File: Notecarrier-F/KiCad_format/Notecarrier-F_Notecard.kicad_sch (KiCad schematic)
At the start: 20 parts, among them J5 NanoSIM - SF72S006VBAR2500, J6 MDT420E01001, SW1 CJS-1200TA, SW2 PTS810SJK250SMTRLFS

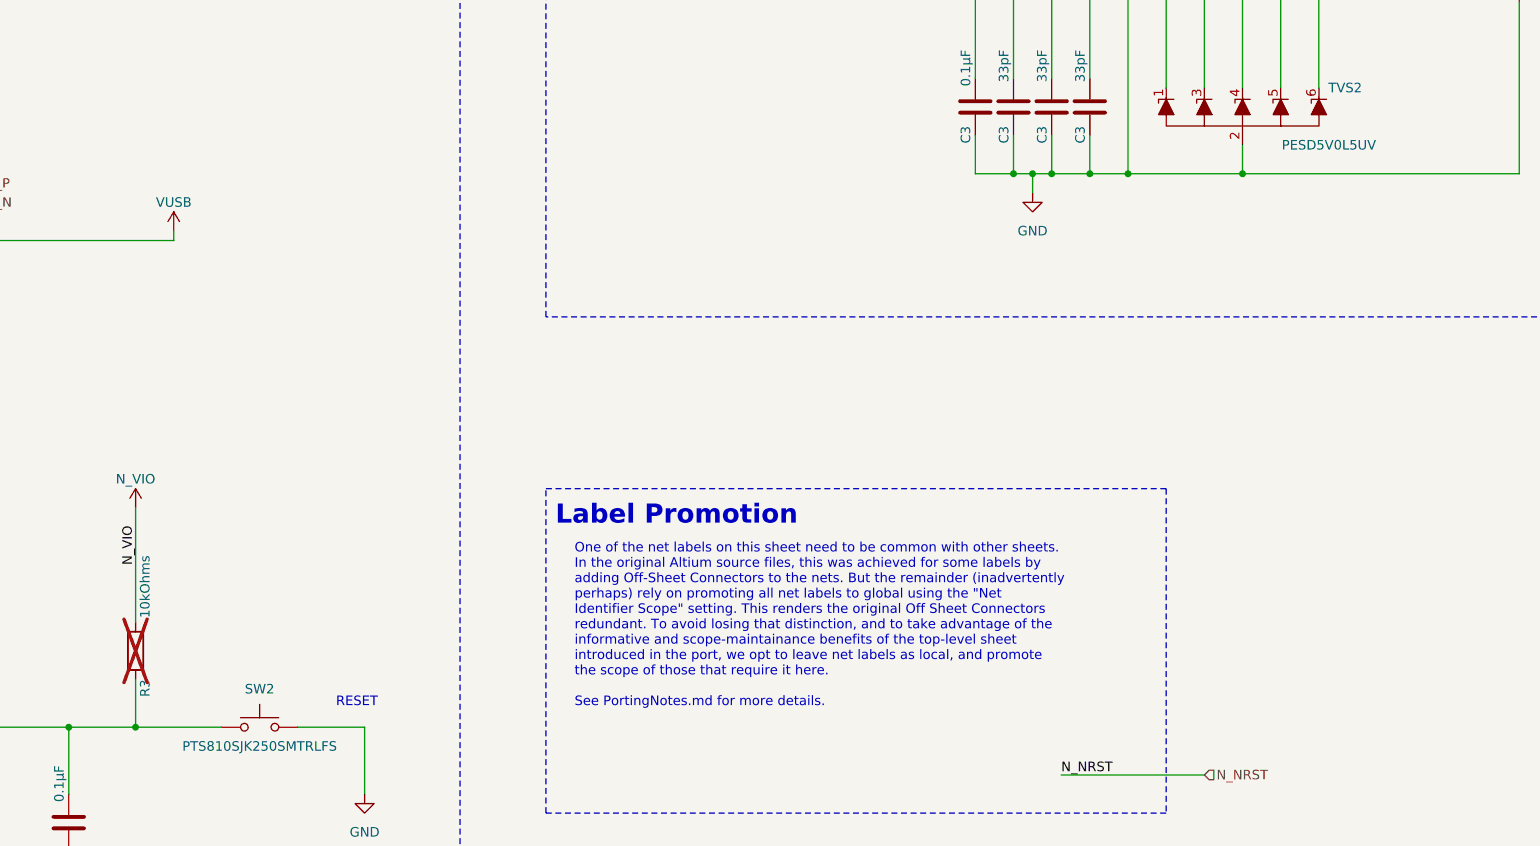
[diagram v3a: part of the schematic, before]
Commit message: Apply first pass validation of Notecarrier-F port
Huge push to identify, solve, document and revalidate all the details revealed by the first run of the validation process. Validation is now acceptable and preparation can be made to release Rev A.
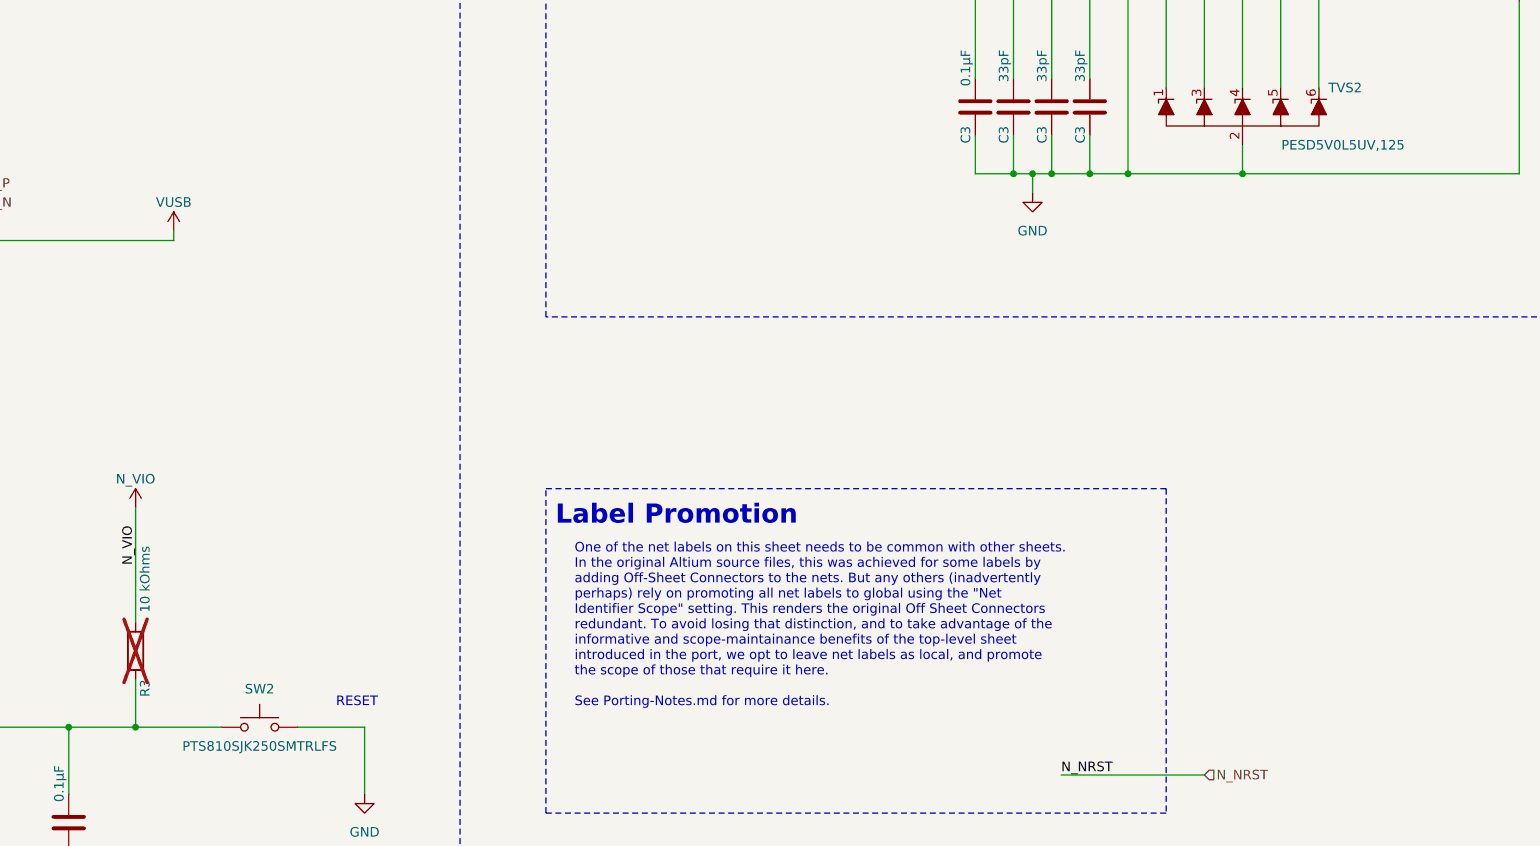
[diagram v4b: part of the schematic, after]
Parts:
- R3: value 10kOhms -> 10 kOhms
- SW2: symbol Switch:SW_Push -> blues-kicad-lib:PTS810-SJS-250-SMTR-LFS
- TVS2: value PESD5V0L5UV -> PESD5V0L5UV,125
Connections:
- net GND: now also SW2.3, SW2.4; no longer SW2.2
- net N_NRST: now also SW2.2
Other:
- note added: "One of the net labels on this sheet needs to be common with other sheets. In the original Altium source files, this was achieved for some labels by adding Off-Sheet Connectors to the nets. But any others (inadvertently perhaps) rely on promoting all net labels to global using the "Net Identifier Scope" setting. This renders the original Off Sheet Connectors redundant. To avoid losing that distinc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"
- note removed: "One of the net labels on this sheet need to be common with other sheets. In the original Altium source files, this was achieved for some labels by adding Off-Sheet Connectors to the nets. But the remainder (inadvertently perhaps) rely on promoting all net labels to global using the "Net Identifier Scope" setting. This renders the original Off Sheet Connectors redundant. To avoid losing that disti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"
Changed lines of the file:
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@@
     (effects (font (size 1.27 1.27)) (justify left bottom))
   )
-  (text "One of the net labels on this sheet need to be common with other sheets.\nIn the original Altium source files, this was achieved for some labels by\nadding Off-Sheet Connectors to the nets. But the remainder (inadvertently\nperhaps) rely on promoting all net labels to global using the \"Net\nIdentifier Scope\" setting. This renders the original Off Sheet Connectors\nredundant. To avoid losing that distinction, and to take advantage of the\ninformative and scope-maintainance benefits of the top-level sheet\nintroduced in the port, we opt to leave net labels as local, and promote\nthe scope of those that require it here.\n\nSee PortingNotes.md for more details."
+  (text "One of the net labels on this sheet needs to be common with other sheets.\nIn the original Altium source files, this was achieved for some labels by\nadding Off-Sheet Connectors to the nets. But any others (inadvertently\nperhaps) rely on promoting all net labels to global using the \"Net\nIdentifier Scope\" setting. This renders the original Off Sheet Connectors\nredundant. To avoid losing that distinction, and to take advantage of the\ninformative and scope-maintainance benefits of the top-level sheet\nintroduced in the port, we opt to leave net labels as local, and promote\nthe scope of those that require it here.\n\nSee Porting-Notes.md for more details."
     (at 247.65 190.5 0)
     (effects (font (size 1.27 1.27)) (justify left bottom))
@@
     )
   )
-  (symbol (lib_id "Switch:SW_Push") (at 205.74 193.04 0) (unit 1)
+  (symbol (lib_id "blues-kicad-lib:PTS810-SJS-250-SMTR-LFS") (at 205.74 193.04 0) (unit 1)
     (in_bom yes) (on_board yes) (dnp no)
     (property "Reference" "SW2" (at 205.74 187.96 0)
@@
     (pin "1")
     (pin "2")
+    (pin "3")
+    (pin "4")
     (instances
       (project "Notecarrier-F"
@@
       (effects (font (size 1.27 1.27)) (justify left))
     )
-    (property "Value" "10kOhms" (at 190.5 170.18 90)
+    (property "Value" "10 kOhms" (at 190.5 168.91 90)
       (effects (font (size 1.27 1.27)) (justify left))
     )
@@
       (effects (font (size 1.27 1.27)) (justify left))
     )
-    (property "Value" "PESD5V0L5UV" (at 354.33 115.57 0)
+    (property "Value" "PESD5V0L5UV,125" (at 358.14 115.57 0)
       (effects (font (size 1.27 1.27)) (justify right))
     )

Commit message: Merge pending library into main.
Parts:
- C3: footprint blues-kicad-lib-pending:CAP 0402_1005 -> blues-kicad-lib:CAP 0402_1005
- J5: footprint blues-kicad-lib-pending:J-NANOSIM-SF72S006VBA -> blues-kicad-lib:J-NANOSIM-SF72S006VBA
- J6: footprint blues-kicad-lib-pending:J-75-0050-MOS-M2 -> blues-kicad-lib:J-75-0050-MOS-M2_with-notecard
- R16, R3, R5: footprint blues-kicad-lib-pending:RES 0402_1005 -> blues-kicad-lib:RES 0402_1005
- RR1, RR2: footprint blues-kicad-lib-pending:RESNET 1506-16 CONVEX -> blues-kicad-lib:RESNET 1506-16 CONVEX
- SW1: footprint blues-kicad-lib-pending:SW_CJS-1200TA -> blues-kicad-lib:SW_CJS-1200TA
- SW2: footprint blues-kicad-lib-pending:C&K PTS810 -> blues-kicad-lib:C&K PTS810
- TVS2: footprint blues-kicad-lib-pending:SOT666 -> blues-kicad-lib:SOT666
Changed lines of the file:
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@@
       (effects (font (size 1.27 1.27)) (justify left))
     )
-    (property "Footprint" "blues-kicad-lib-pending:CAP 0402_1005" (at 300.0248 106.68 0)
+    (property "Footprint" "blues-kicad-lib:CAP 0402_1005" (at 300.0248 106.68 0)
       (effects (font (size 1.27 1.27)) hide)
     )
@@
       (effects (font (size 1.27 1.27)) (justify left))
     )
-    (property "Footprint" "blues-kicad-lib-pending:CAP 0402_1005" (at 310.1848 106.68 0)
+    (property "Footprint" "blues-kicad-lib:CAP 0402_1005" (at 310.1848 106.68 0)
       (effects (font (size 1.27 1.27)) hide)
     )
@@
       (effects (font (size 1.27 1.27)))
     )
-    (property "Footprint" "blues-kicad-lib-pending:C&K PTS810" (at 205.74 187.96 0)
+    (property "Footprint" "blues-kicad-lib:C&K PTS810" (at 205.74 187.96 0)
       (effects (font (size 1.27 1.27)) hide)
     )
@@
       (effects (font (size 1.27 1.27)) (justify left))
     )
-    (property "Footprint" "blues-kicad-lib-pending:CAP 0402_1005" (at 315.2648 106.68 0)
+    (property "Footprint" "blues-kicad-lib:CAP 0402_1005" (at 315.2648 106.68 0)
       (effects (font (size 1.27 1.27)) hide)
     )
@@
       (effects (font (size 1.27 1.27)) (justify left))
     )
-    (property "Footprint" "blues-kicad-lib-pending:CAP 0402_1005" (at 179.3748 201.93 0)
+    (property "Footprint" "blues-kicad-lib:CAP 0402_1005" (at 179.3748 201.93 0)
       (effects (font (size 1.27 1.27)) hide)
     )
@@
       (effects (font (size 1.27 1.27)) (justify left))
     )
-    (property "Footprint" "blues-kicad-lib-pending:RES 0402_1005" (at 278.13 68.072 90)
+    (property "Footprint" "blues-kicad-lib:RES 0402_1005" (at 278.13 68.072 90)
       (effects (font (size 1.27 1.27)) hide)
     )
@@
       (effects (font (size 1.27 1.27)) (justify left))
     )
-    (property "Footprint" "blues-kicad-lib-pending:RES 0402_1005" (at 278.13 70.612 90)
+    (property "Footprint" "blues-kicad-lib:RES 0402_1005" (at 278.13 70.612 90)
       (effects (font (size 1.27 1.27)) hide)
     )
@@
       (effects (font (size 1.27 1.27)))
     )
-    (property "Footprint" "blues-kicad-lib-pending:J-75-0050-MOS-M2" (at 137.16 210.82 0)
+    (property "Footprint" "blues-kicad-lib:J-75-0050-MOS-M2_with-notecard" (at 137.16 210.82 0)
       (effects (font (size 1.27 1.27)) hide)
     )
@@
     )
     (property "Supplier" "Digi-Key" (at 134.62 157.48 0)
+      (effects (font (size 1.27 1.27)) hide)
+    )
+    (property "Critical" "" (at 134.62 157.48 0)
       (effects (font (size 1.27 1.27)) hide)
     )
@@
       (effects (font (size 1.27 1.27)) (justify left))
     )
-    (property "Footprint" "blues-kicad-lib-pending:CAP 0402_1005" (at 305.1048 106.68 0)
+    (property "Footprint" "blues-kicad-lib:CAP 0402_1005" (at 305.1048 106.68 0)
       (effects (font (size 1.27 1.27)) hide)
     )
@@
       (effects (font (size 1.27 1.27)) (justify left))
     )
-    (property "Footprint" "blues-kicad-lib-pending:J-NANOSIM-SF72S006VBA" (at 361.95 106.68 0)
+    (property "Footprint" "blues-kicad-lib:J-NANOSIM-SF72S006VBA" (at 361.95 106.68 0)
       (effects (font (size 1.27 1.27)) hide)
     )
@@
       (effects (font (size 1.27 1.27)) (justify right))
     )
-    (property "Footprint" "blues-kicad-lib-pending:RES 0402_1005" (at 295.148 59.69 90)
+    (property "Footprint" "blues-kicad-lib:RES 0402_1005" (at 295.148 59.69 90)
       (effects (font (size 1.27 1.27)) hide)
     )
@@
       (effects (font (size 1.27 1.27)) (justify left))
     )
-    (property "Footprint" "blues-kicad-lib-pending:RES 0402_1005" (at 278.13 80.772 90)
+    (property "Footprint" "blues-kicad-lib:RES 0402_1005" (at 278.13 80.772 90)
       (effects (font (size 1.27 1.27)) hide)
     )
@@
       (effects (font (size 1.27 1.27)) (justify left))
     )
-    (property "Footprint" "blues-kicad-lib-pending:RES 0402_1005" (at 191.008 182.88 90)
+    (property "Footprint" "blues-kicad-lib:RES 0402_1005" (at 191.008 182.88 90)
       (effects (font (size 1.27 1.27)) hide)
     )
@@
       (effects (font (size 1.27 1.27)))
     )
-    (property "Footprint" "blues-kicad-lib-pending:RESNET 1506-16 CONVEX" (at 52.07 195.834 0)
+    (property "Footprint" "blues-kicad-lib:RESNET 1506-16 CONVEX" (at 52.07 195.834 0)
       (effects (font (size 1.27 1.27)) hide)
     )
@@
       (effects (font (size 1.27 1.27)) (justify right))
     )
-    (property "Footprint" "blues-kicad-lib-pending:SOT666" (at 336.55 123.19 0)
+    (property "Footprint" "blues-kicad-lib:SOT666" (at 336.55 123.19 0)
       (effects (font (size 1.27 1.27)) hide)
     )
@@
       (effects (font (size 1.27 1.27)))
     )
-    (property "Footprint" "blues-kicad-lib-pending:RESNET 1506-16 CONVEX" (at 71.12 195.834 0)
+    (property "Footprint" "blues-kicad-lib:RESNET 1506-16 CONVEX" (at 71.12 195.834 0)
       (effects (font (size 1.27 1.27)) hide)
     )
@@
     )
   )
-  (symbol (lib_name "CJS-1200TA_1") (lib_id "blues-kicad-lib:CJS-1200TA") (at 73.66 135.89 0) (mirror y) (unit 1)
+  (symbol (lib_id "blues-kicad-lib:CJS-1200TA") (at 73.66 135.89 0) (mirror y) (unit 1)
     (in_bom yes) (on_board yes) (dnp no)
     (property "Reference" "SW1" (at 73.66 130.81 0)
@@
       (effects (font (size 1.27 1.27)))
     )
-    (property "Footprint" "blues-kicad-lib-pending:SW_CJS-1200TA" (at 73.66 143.51 0)
-      (effects (font (size 1.27 1.27)) hide)
-    )
+    (property "Footprint" "blues-kicad-lib:SW_CJS-1200TA" (at 73.66 143.51 0)
+      (effects (font (size 1.27 1.27)) hide)
+    )
